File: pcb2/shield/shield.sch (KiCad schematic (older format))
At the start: 17 parts, among them IC1 AM26C31CNSR, IC2 AM26C31CNSR, P1 ARD_NW, P10 BUS5, P11 BUS6, P12 BUS7, P13 BUS8, P2 ARD_SW, P3 ARD_NE, P4 ARD_SE, P5 SHIFT, P6 BUS1, P7 BUS2, P8 BUS3, P9 BUS4

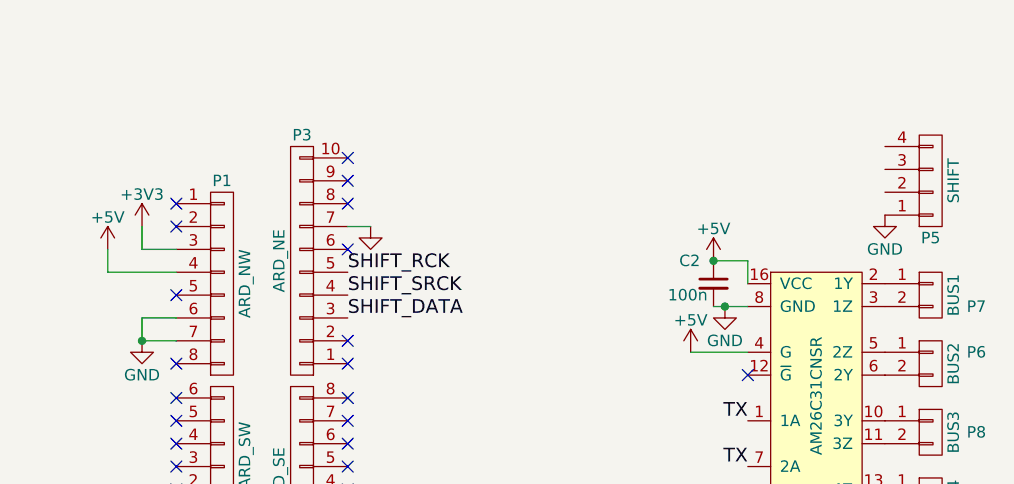
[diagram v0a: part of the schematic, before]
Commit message: Added SHIFT connections, sated ERC
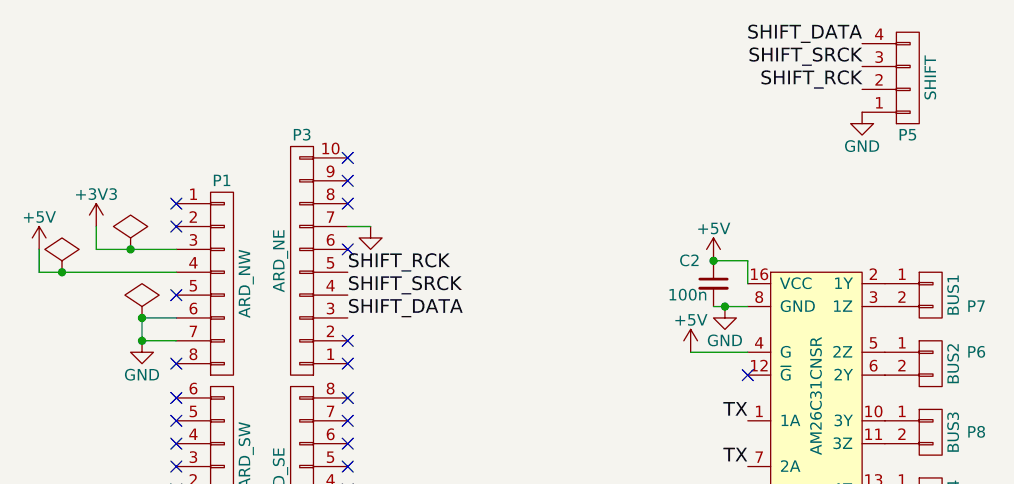
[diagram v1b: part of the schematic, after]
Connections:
- net SHIFT_DATA: now also P5.4 (P4)
- net SHIFT_RCK: now also P5.2 (P2)
- net SHIFT_SRCK: now also P5.3 (P3)
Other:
- moved on the sheet: P5
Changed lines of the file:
@@
 L +3V3 #PWR01
 U 1 1 56F8546D
-P 2150 2000
-F 0 "#PWR01" H 2150 1850 50  0001 C CNN
-F 1 "+3V3" H 2150 2140 50  0000 C CNN
-F 2 "" H 2150 2000 50  0000 C CNN
-F 3 "" H 2150 2000 50  0000 C CNN
-	1    2150 2000
-	1    0    0    -1
-$EndComp
-Wire Wire Line
-	2150 2000 2150 2100
-Wire Wire Line
-	2150 2100 2300 2100
+P 1950 2000
+F 0 "#PWR01" H 1950 1850 50  0001 C CNN
+F 1 "+3V3" H 1950 2140 50  0000 C CNN
+F 2 "" H 1950 2000 50  0000 C CNN
+F 3 "" H 1950 2000 50  0000 C CNN
+	1    1950 2000
+	1    0    0    -1
+$EndComp
+Wire Wire Line
+	1950 2000 1950 2100
+Wire Wire Line
+	1950 2100 2300 2100
 $Comp
 L +5V #PWR02
 U 1 1 56F85493
-P 2000 2100
-F 0 "#PWR02" H 2000 1950 50  0001 C CNN
-F 1 "+5V" H 2000 2240 50  0000 C CNN
-F 2 "" H 2000 2100 50  0000 C CNN
-F 3 "" H 2000 2100 50  0000 C CNN
-	1    2000 2100
-	1    0    0    -1
-$EndComp
-Wire Wire Line
-	2000 2100 2000 2200
-Wire Wire Line
-	2000 2200 2300 2200
+P 1700 2100
+F 0 "#PWR02" H 1700 1950 50  0001 C CNN
+F 1 "+5V" H 1700 2240 50  0000 C CNN
+F 2 "" H 1700 2100 50  0000 C CNN
+F 3 "" H 1700 2100 50  0000 C CNN
+	1    1700 2100
+	1    0    0    -1
+$EndComp
+Wire Wire Line
+	1700 2100 1700 2200
+Wire Wire Line
+	1700 2200 2300 2200
 $Comp
 L GND #PWR03
@@
 L CONN_01X04 P5
 U 1 1 56F855FD
-P 5600 1800
-F 0 "P5" H 5600 2050 50  0000 C CNN
-F 1 "SHIFT" V 5700 1800 50  0000 C CNN
-F 2 "Pin_Headers:Pin_Header_Straight_1x04" H 5600 1800 50  0001 C CNN
-F 3 "" H 5600 1800 50  0000 C CNN
-	1    5600 1800
+P 5500 1350
+F 0 "P5" H 5500 1600 50  0000 C CNN
+F 1 "SHIFT" V 5600 1350 50  0000 C CNN
+F 2 "Pin_Headers:Pin_Header_Straight_1x04" H 5500 1350 50  0001 C CNN
+F 3 "" H 5500 1350 50  0000 C CNN
+	1    5500 1350
 	1    0    0    1
 $EndComp
@@
 L GND #PWR05
 U 1 1 56F85F2A
-P 5400 1950
-F 0 "#PWR05" H 5400 1700 50  0001 C CNN
-F 1 "GND" H 5400 1800 50  0000 C CNN
-F 2 "" H 5400 1950 50  0000 C CNN
-F 3 "" H 5400 1950 50  0000 C CNN
-	1    5400 1950
+P 5300 1500
+F 0 "#PWR05" H 5300 1250 50  0001 C CNN
+F 1 "GND" H 5300 1350 50  0000 C CNN
+F 2 "" H 5300 1500 50  0000 C CNN
+F 3 "" H 5300 1500 50  0000 C CNN
+	1    5300 1500
 	1    0    0    -1
 $EndComp
@@
 	4550 3500 4550 3600
 Connection ~ 4700 3700
+Text Label 5300 1400 2    60   ~ 0
+SHIFT_RCK
+Text Label 5300 1300 2    60   ~ 0
+SHIFT_SRCK
+Text Label 5300 1200 2    60   ~ 0
+SHIFT_DATA
+$Comp
+L PWR_FLAG #FLG012
+U 1 1 56F87626
+P 2100 2100
+F 0 "#FLG012" H 2100 2195 50  0001 C CNN
+F 1 "PWR_FLAG" H 2100 2280 50  0001 C CNN
+F 2 "" H 2100 2100 50  0000 C CNN
+F 3 "" H 2100 2100 50  0000 C CNN
+	1    2100 2100
+	1    0    0    -1
+$EndComp
+Connection ~ 2100 2100
+$Comp
+L PWR_FLAG #FLG013
+U 1 1 56F87848
+P 2150 2400
+F 0 "#FLG013" H 2150 2495 50  0001 C CNN
+F 1 "PWR_FLAG" H 2150 2580 50  0001 C CNN
+F 2 "" H 2150 2400 50  0000 C CNN
+F 3 "" H 2150 2400 50  0000 C CNN
+	1    2150 2400
+	1    0    0    -1
+$EndComp
+Connection ~ 2150 2400
+$Comp
+L PWR_FLAG #FLG014
+U 1 1 56F87AC1
+P 1800 2200
+F 0 "#FLG014" H 1800 2295 50  0001 C CNN
+F 1 "PWR_FLAG" H 1800 2380 50  0001 C CNN
+F 2 "" H 1800 2200 50  0000 C CNN
+F 3 "" H 1800 2200 50  0000 C CNN
+	1    1800 2200
+	1    0    0    -1
+$EndComp
+Connection ~ 1800 2200
 $EndSCHEMATC

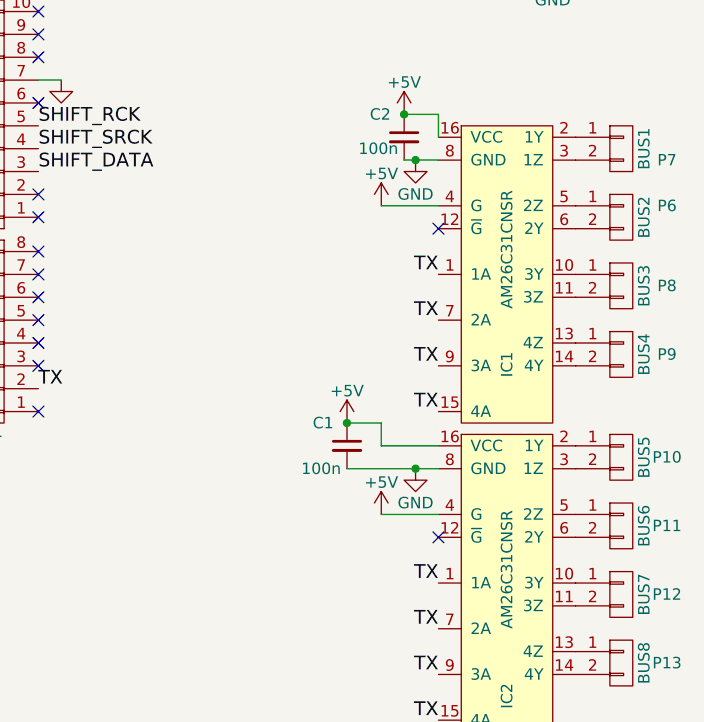
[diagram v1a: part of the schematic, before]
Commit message: Proof of concept route of shield
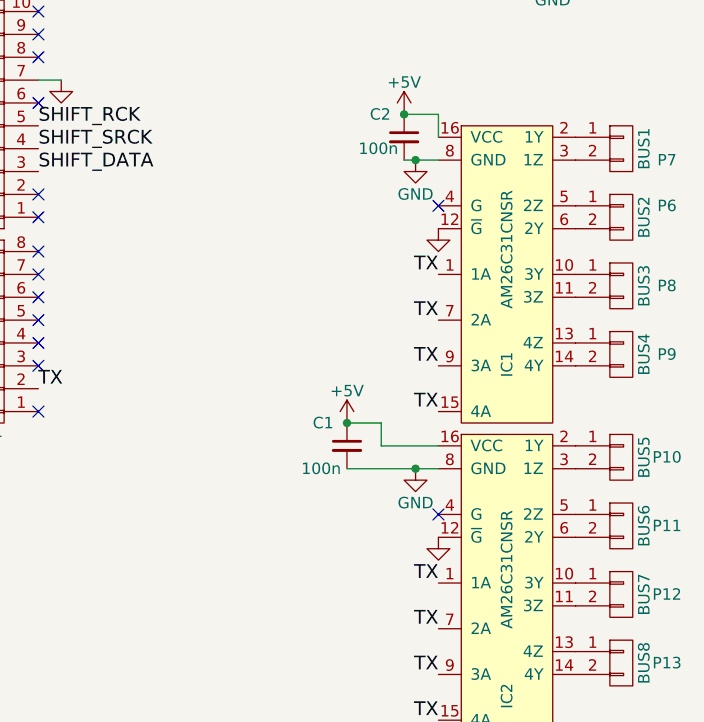
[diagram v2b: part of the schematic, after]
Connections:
- net +5V: no longer IC1.4 (G), IC2.4 (G)
- net GND: now also IC1.12 (~G), IC2.12 (~G)
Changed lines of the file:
@@
 Wire Wire Line
 	4650 2350 4800 2350
-Wire Wire Line
-	4800 2550 4550 2550
-$Comp
-L +5V #PWR08
-U 1 1 56F86E14
-P 4550 2550
-F 0 "#PWR08" H 4550 2400 50  0001 C CNN
-F 1 "+5V" H 4550 2690 50  0000 C CNN
-F 2 "" H 4550 2550 50  0000 C CNN
-F 3 "" H 4550 2550 50  0000 C CNN
-	1    4550 2550
-	1    0    0    -1
-$EndComp
 $Comp
 L +5V #PWR09
@@
 Wire Wire Line
 	4400 3700 4800 3700
-Wire Wire Line
-	4800 3900 4550 3900
-$Comp
-L +5V #PWR011
-U 1 1 56F86F7D
-P 4550 3900
-F 0 "#PWR011" H 4550 3750 50  0001 C CNN
-F 1 "+5V" H 4550 4040 50  0000 C CNN
-F 2 "" H 4550 3900 50  0000 C CNN
-F 3 "" H 4550 3900 50  0000 C CNN
-	1    4550 3900
-	1    0    0    -1
-$EndComp
-NoConn ~ 4800 2650
-NoConn ~ 4800 4000
 Text Label 4800 2850 2    60   ~ 0
 TX
@@
 $EndComp
 Connection ~ 1800 2200
+NoConn ~ 4800 2550
+$Comp
+L GND #PWR?
+U 1 1 56F87C8E
+P 4800 2650
+F 0 "#PWR?" H 4800 2400 50  0001 C CNN
+F 1 "GND" H 4800 2500 50  0001 C CNN
+F 2 "" H 4800 2650 50  0000 C CNN
+F 3 "" H 4800 2650 50  0000 C CNN
+	1    4800 2650
+	1    0    0    -1
+$EndComp
+$Comp
+L GND #PWR?
+U 1 1 56F87D9A
+P 4800 4000
+F 0 "#PWR?" H 4800 3750 50  0001 C CNN
+F 1 "GND" H 4800 3850 50  0001 C CNN
+F 2 "" H 4800 4000 50  0000 C CNN
+F 3 "" H 4800 4000 50  0000 C CNN
+	1    4800 4000
+	1    0    0    -1
+$EndComp
+NoConn ~ 4800 3900
 $EndSCHEMATC

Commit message: Added part numbers and BOMs
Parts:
- C1, C2: Farnell (none) -> 2496833
- P10, P11, P12, P13, P6, P7, P8, P9: Farnell (none) -> 1830747
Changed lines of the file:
@@
 F 2 "agg:S02B-PASK-2" H 5600 2300 50  0001 C CNN
 F 3 "" H 5600 2300 50  0000 C CNN
+F 4 "1830747" H 5600 2300 60  0001 C CNN "Farnell"
 	1    5600 2300
 	1    0    0    -1
@@
 F 2 "agg:S02B-PASK-2" H 5600 2600 50  0001 C CNN
 F 3 "" H 5600 2600 50  0000 C CNN
+F 4 "1830747" H 5600 2600 60  0001 C CNN "Farnell"
 	1    5600 2600
 	1    0    0    -1
@@
 F 2 "agg:S02B-PASK-2" H 5600 2900 50  0001 C CNN
 F 3 "" H 5600 2900 50  0000 C CNN
+F 4 "1830747" H 5600 2900 60  0001 C CNN "Farnell"
 	1    5600 2900
 	1    0    0    -1
@@
 F 2 "agg:S02B-PASK-2" H 5600 3200 50  0001 C CNN
 F 3 "" H 5600 3200 50  0000 C CNN
+F 4 "1830747" H 5600 3200 60  0001 C CNN "Farnell"
 	1    5600 3200
 	1    0    0    -1
@@
 F 2 "agg:S02B-PASK-2" H 5600 3650 50  0001 C CNN
 F 3 "" H 5600 3650 50  0000 C CNN
+F 4 "1830747" H 5600 3650 60  0001 C CNN "Farnell"
 	1    5600 3650
 	1    0    0    -1
@@
 F 2 "agg:S02B-PASK-2" H 5600 3950 50  0001 C CNN
 F 3 "" H 5600 3950 50  0000 C CNN
+F 4 "1830747" H 5600 3950 60  0001 C CNN "Farnell"
 	1    5600 3950
 	1    0    0    -1
@@
 F 2 "agg:S02B-PASK-2" H 5600 4250 50  0001 C CNN
 F 3 "" H 5600 4250 50  0000 C CNN
+F 4 "1830747" H 5600 4250 60  0001 C CNN "Farnell"
 	1    5600 4250
 	1    0    0    -1
@@
 F 2 "agg:S02B-PASK-2" H 5600 4550 50  0001 C CNN
 F 3 "" H 5600 4550 50  0000 C CNN
+F 4 "1830747" H 5600 4550 60  0001 C CNN "Farnell"
 	1    5600 4550
 	1    0    0    -1
@@
 F 2 "agg:0603" H 4650 2250 50  0001 C CNN
 F 3 "" H 4650 2250 50  0000 C CNN
+F 4 "2496833" H 4650 2250 60  0001 C CNN "Farnell"
 	1    4650 2250
 	1    0    0    -1
@@
 F 2 "agg:0603" H 4400 3600 50  0001 C CNN
 F 3 "" H 4400 3600 50  0000 C CNN
+F 4 "2496833" H 4400 3600 60  0001 C CNN "Farnell"
 	1    4400 3600
 	1    0    0    -1

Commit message: Repsin of new shield PCB, nominal first route.
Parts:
- removed IC1, IC2: AM26C31CNSR, agg:SOIC-16, symbol AM26C31CNSR
- removed P1: ARD_NW, Pin_Headers:Pin_Header_Straight_1x08, symbol CONN_01X08
- removed P2: ARD_SW, Pin_Headers:Pin_Header_Straight_1x06, symbol CONN_01X06
- removed P3: ARD_NE, Pin_Headers:Pin_Header_Straight_1x10, symbol CONN_01X10
- removed P4: ARD_SE, Pin_Headers:Pin_Header_Straight_1x08, symbol CONN_01X08
- added C10, C7, C9: 1u, agg:0603, symbol C
- added C3, C6, C8: 100n, agg:0603, symbol C
- added C4: 10u, agg:0603, symbol C
- added C5: C, agg:0603, symbol C
- added IC1: STM32F0xxKxTx, agg:LQFP-32, symbol STM32F0xxKxTx
- added IC2: MCP1700, agg:SOT-23, symbol MCP1700
- added IC3, IC4: AM26C31, agg:SOIC-16, symbol AM26C31
- added J1: MICROUSB, agg:MICROUSB_MOLEX_47589-0001, symbol MICROUSB
- added P?: SWD_TC, agg:TC2030-NL, symbol SWD_TC
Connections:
- net +3V3: now also C10.1, C3.1, C4.1, C6.1, C7.1, C8.1, IC1.1 (VDD), IC1.17 (VDD), IC1.5 (VDDA), IC2.2 (VOUT), P?.1 (VDD)
- net +5V: now also C9.1, IC2.3 (VIN), IC3.16 (VCC), IC4.16 (VCC), J1.1 (VCC)
- net GND: now also C10.2, C3.2, C4.2, C5.2, C6.2, C7.2, C8.2, C9.2, IC1.16 (VSS), IC1.31 (BOOT0), IC1.32 (VSS), IC2.1 (GND), IC3.12 (~G), IC3.8 (GND), IC4.12 (~G), IC4.8 (GND), J1.5 (GND), P?.5 (GND)
- net SHIFT_DATA: now also IC1.13 (PA7)
- net SHIFT_RCK: now also IC1.11 (PA5)
- net SHIFT_SRCK: now also IC1.12 (PA6)
- net TX: now also IC1.8 (PA2), IC3.1 (1A), IC3.15 (4A), IC3.7 (2A), IC3.9 (3A), IC4.1 (1A), IC4.15 (4A), IC4.7 (2A), IC4.9 (3A)
- net at P6.1 (P1): now also IC3.2 (1Y)
- net at P6.2 (P2): now also IC3.3 (1Z)
- net at P7.1 (P1): now also IC3.6 (2Y)
- net at P7.2 (P2): now also IC3.5 (2Z)
- net at P8.1 (P1): now also IC3.10 (3Y)
- net at P8.2 (P2): now also IC3.11 (3Z)
- net at P9.1 (P1): now also IC3.14 (4Y)
- net at P9.2 (P2): now also IC3.13 (4Z)
- net at P10.1 (P1): now also IC4.2 (1Y)
- net at P10.2 (P2): now also IC4.3 (1Z)
- net at P11.1 (P1): now also IC4.6 (2Y)
- net at P11.2 (P2): now also IC4.5 (2Z)
- net at P12.1 (P1): now also IC4.10 (3Y)
- net at P12.2 (P2): now also IC4.11 (3Z)
- net at P13.1 (P1): now also IC4.14 (4Y)
- net at P13.2 (P2): now also IC4.13 (4Z)
- new net SWDCLK: IC1.24 (PA14), P?.4 (SWDCLK)
- new net SWDIO: IC1.23 (PA13), P?.2 (SWDIO)
- new net USB_D+: IC1.22 (PA12), J1.3 (D+)
- new net USB_D-: IC1.21 (PA11), J1.2 (D-)
- new net nRST: C5.1, IC1.4 (NRST), P?.3 (~RST)
- no-connect marks 25 -> 5
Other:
- note added: "VDD1"
- note added: "VDD2"
- note added: "VDDA"
- moved on the sheet: C1, C2, P10, P11, P12, P13, P5, P6, P7, P8, P9

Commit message: Re-route of shield, DRC issues though.
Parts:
- added X1, X2, X3, X4: PART, agg:M3_MOUNT, symbol PART
- gave numbers to parts that had none: 1
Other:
- note added: "Mounting\nHoles"
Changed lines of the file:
@@
 LIBS:mcp1700
 LIBS:swd_tc
+LIBS:part
 LIBS:shield-cache
 EELAYER 25 0
@@
 $EndComp
 $Comp
-L GND #PWR01
+L GND #PWR30
 U 1 1 56F85F2A
 P 8850 1650
-F 0 "#PWR01" H 8850 1400 50  0001 C CNN
+F 0 "#PWR30" H 8850 1400 50  0001 C CNN
 F 1 "GND" H 8850 1500 50  0000 C CNN
 F 2 "" H 8850 1650 50  0000 C CNN
@@
 $EndComp
 $Comp
-L +5V #PWR02
+L +5V #PWR25
 U 1 1 56F86D5E
 P 8200 2300
-F 0 "#PWR02" H 8200 2150 50  0001 C CNN
+F 0 "#PWR25" H 8200 2150 50  0001 C CNN
 F 1 "+5V" H 8200 2440 50  0000 C CNN
 F 2 "" H 8200 2300 50  0000 C CNN
@@
 $EndComp
 $Comp
-L GND #PWR03
+L GND #PWR26
 U 1 1 56F86DAA
 P 8250 2500
-F 0 "#PWR03" H 8250 2250 50  0001 C CNN
+F 0 "#PWR26" H 8250 2250 50  0001 C CNN
 F 1 "GND" H 8250 2350 50  0000 C CNN
 F 2 "" H 8250 2500 50  0000 C CNN
@@
 $EndComp
 $Comp
-L +5V #PWR04
+L +5V #PWR24
 U 1 1 56F86E73
 P 7950 3900
-F 0 "#PWR04" H 7950 3750 50  0001 C CNN
+F 0 "#PWR24" H 7950 3750 50  0001 C CNN
 F 1 "+5V" H 7950 4040 50  0000 C CNN
 F 2 "" H 7950 3900 50  0000 C CNN
@@
 $EndComp
 $Comp
-L GND #PWR05
+L GND #PWR27
 U 1 1 56F86EC2
 P 8250 4100
-F 0 "#PWR05" H 8250 3850 50  0001 C CNN
+F 0 "#PWR27" H 8250 3850 50  0001 C CNN
 F 1 "GND" H 8250 3950 50  0000 C CNN
 F 2 "" H 8250 4100 50  0000 C CNN
@@
 NoConn ~ 8350 2700
 $Comp
-L GND #PWR06
+L GND #PWR28
 U 1 1 56F87C8E
 P 8350 2800
-F 0 "#PWR06" H 8350 2550 50  0001 C CNN
+F 0 "#PWR28" H 8350 2550 50  0001 C CNN
 F 1 "GND" H 8350 2650 50  0001 C CNN
 F 2 "" H 8350 2800 50  0000 C CNN
@@
 $EndComp
 $Comp
-L GND #PWR07
+L GND #PWR29
 U 1 1 56F87D9A
 P 8350 4400
-F 0 "#PWR07" H 8350 4150 50  0001 C CNN
+F 0 "#PWR29" H 8350 4150 50  0001 C CNN
 F 1 "GND" H 8350 4250 50  0001 C CNN
 F 2 "" H 8350 4400 50  0000 C CNN
@@
 $EndComp
 $Comp
-L +5V #PWR08
+L +5V #PWR15
 U 1 1 5794B897
 P 4550 1300
-F 0 "#PWR08" H 4550 1150 50  0001 C CNN
+F 0 "#PWR15" H 4550 1150 50  0001 C CNN
 F 1 "+5V" H 4565 1473 50  0000 C CNN
 F 2 "" H 4550 1300 50  0000 C CNN
@@
 $EndComp
 $Comp
-L GND #PWR09
+L GND #PWR16
 U 1 1 5794B8F4
 P 4600 1950
-F 0 "#PWR09" H 4600 1700 50  0001 C CNN
+F 0 "#PWR16" H 4600 1700 50  0001 C CNN
 F 1 "GND" H 4605 1777 50  0000 C CNN
 F 2 "" H 4600 1950 50  0000 C CNN
@@
 $EndComp
 $Comp
-L +3V3 #PWR010
+L +3V3 #PWR12
 U 1 1 5794BB55
 P 2500 3200
-F 0 "#PWR010" H 2500 3050 50  0001 C CNN
+F 0 "#PWR12" H 2500 3050 50  0001 C CNN
 F 1 "+3V3" H 2515 3373 50  0000 C CNN
 F 2 "" H 2500 3200 50  0000 C CNN
@@
 $EndComp
 $Comp
-L GND #PWR011
+L GND #PWR9
 U 1 1 5794BBFE
 P 2400 3550
-F 0 "#PWR011" H 2400 3300 50  0001 C CNN
+F 0 "#PWR9" H 2400 3300 50  0001 C CNN
 F 1 "GND" H 2405 3377 50  0000 C CNN
 F 2 "" H 2400 3550 50  0000 C CNN
@@
 $EndComp
 $Comp
-L GND #PWR012
+L GND #PWR5
 U 1 1 5794BE19
 P 1850 4150
-F 0 "#PWR012" H 1850 3900 50  0001 C CNN
+F 0 "#PWR5" H 1850 3900 50  0001 C CNN
 F 1 "GND" H 1855 3977 50  0000 C CNN
 F 2 "" H 1850 4150 50  0000 C CNN
@@
 nRST
 $Comp
-L GND #PWR013
+L GND #PWR8
 U 1 1 5794BF98
 P 2150 3950
-F 0 "#PWR013" H 2150 3700 50  0001 C CNN
+F 0 "#PWR8" H 2150 3700 50  0001 C CNN
 F 1 "GND" H 2155 3777 50  0000 C CNN
 F 2 "" H 2150 3950 50  0000 C CNN
@@
 $EndComp
 $Comp
-L +3V3 #PWR014
+L +3V3 #PWR1
 U 1 1 5794C2DC
 P 1350 900
-F 0 "#PWR014" H 1350 750 50  0001 C CNN
+F 0 "#PWR1" H 1350 750 50  0001 C CNN
 F 1 "+3V3" H 1365 1073 50  0000 C CNN
 F 2 "" H 1350 900 50  0000 C CNN
@@
 $EndComp
 $Comp
-L +3V3 #PWR015
+L +3V3 #PWR3
 U 1 1 5794C329
 P 1750 900
-F 0 "#PWR015" H 1750 750 50  0001 C CNN
+F 0 "#PWR3" H 1750 750 50  0001 C CNN
 F 1 "+3V3" H 1765 1073 50  0000 C CNN
 F 2 "" H 1750 900 50  0000 C CNN
@@
 $EndComp
 $Comp
-L +3V3 #PWR016
+L +3V3 #PWR6
 U 1 1 5794C376
 P 2100 900
-F 0 "#PWR016" H 2100 750 50  0001 C CNN
+F 0 "#PWR6" H 2100 750 50  0001 C CNN
 F 1 "+3V3" H 2115 1073 50  0000 C CNN
 F 2 "" H 2100 900 50  0000 C CNN
@@
 $EndComp
 $Comp
-L GND #PWR017
+L GND #PWR2
 U 1 1 5794C3C3
 P 1350 1200
-F 0 "#PWR017" H 1350 950 50  0001 C CNN
+F 0 "#PWR2" H 1350 950 50  0001 C CNN
 F 1 "GND" H 1355 1027 50  0000 C CNN
 F 2 "" H 1350 1200 50  0000 C CNN
@@
 $EndComp
 $Comp
-L GND #PWR018
+L GND #PWR4
 U 1 1 5794C410
 P 1750 1200
-F 0 "#PWR018" H 1750 950 50  0001 C CNN
+F 0 "#PWR4" H 1750 950 50  0001 C CNN
 F 1 "GND" H 1755 1027 50  0000 C CNN
 F 2 "" H 1750 1200 50  0000 C CNN
@@
 $EndComp
 $Comp
-L GND #PWR019
+L GND #PWR7
 U 1 1 5794C45D
 P 2100 1200
-F 0 "#PWR019" H 2100 950 50  0001 C CNN
+F 0 "#PWR7" H 2100 950 50  0001 C CNN
 F 1 "GND" H 2105 1027 50  0000 C CNN
 F 2 "" H 2100 1200 50  0000 C CNN
@@
 $EndComp
 $Comp
-L +3V3 #PWR020
+L +3V3 #PWR10
 U 1 1 5794C73B
 P 2500 900
-F 0 "#PWR020" H 2500 750 50  0001 C CNN
+F 0 "#PWR10" H 2500 750 50  0001 C CNN
 F 1 "+3V3" H 2515 1073 50  0000 C CNN
 F 2 "" H 2500 900 50  0000 C CNN
@@
 $EndComp
 $Comp
-L +3V3 #PWR021
+L +3V3 #PWR13
 U 1 1 5794C78E
 P 2800 900
-F 0 "#PWR021" H 2800 750 50  0001 C CNN
+F 0 "#PWR13" H 2800 750 50  0001 C CNN
 F 1 "+3V3" H 2815 1073 50  0000 C CNN
 F 2 "" H 2800 900 50  0000 C CNN
@@
 $EndComp
 $Comp
-L GND #PWR022
+L GND #PWR11
 U 1 1 5794C7E1
 P 2500 1200
-F 0 "#PWR022" H 2500 950 50  0001 C CNN
+F 0 "#PWR11" H 2500 950 50  0001 C CNN
 F 1 "GND" H 2505 1027 50  0000 C CNN
 F 2 "" H 2500 1200 50  0000 C CNN
@@
 $EndComp
 $Comp
-L GND #PWR023
+L GND #PWR14
 U 1 1 5794C834
 P 2800 1200
-F 0 "#PWR023" H 2800 950 50  0001 C CNN
+F 0 "#PWR14" H 2800 950 50  0001 C CNN
 F 1 "GND" H 2805 1027 50  0000 C CNN
 F 2 "" H 2800 1200 50  0000 C CNN
@@
 $EndComp
 $Comp
-L GND #PWR024
+L GND #PWR21
 U 1 1 5794D178
 P 6000 1450
-F 0 "#PWR024" H 6000 1200 50  0001 C CNN
+F 0 "#PWR21" H 6000 1200 50  0001 C CNN
 F 1 "GND" H 6005 1277 50  0000 C CNN
 F 2 "" H 6000 1450 50  0000 C CNN
@@
 	2150 3950 2600 3950
 $Comp
-L +5V #PWR025
+L +5V #PWR19
 U 1 1 5794D32F
 P 5600 1350
-F 0 "#PWR025" H 5600 1200 50  0001 C CNN
+F 0 "#PWR19" H 5600 1200 50  0001 C CNN
 F 1 "+5V" H 5615 1523 50  0000 C CNN
 F 2 "" H 5600 1350 50  0000 C CNN
@@
 Connection ~ 5600 1350
 $Comp
-L GND #PWR026
+L GND #PWR20
 U 1 1 5794D41F
 P 5600 1650
-F 0 "#PWR026" H 5600 1400 50  0001 C CNN
+F 0 "#PWR20" H 5600 1400 50  0001 C CNN
 F 1 "GND" H 5605 1477 50  0000 C CNN
 F 2 "" H 5600 1650 50  0000 C CNN
@@
 $EndComp
 $Comp
-L +3V3 #PWR027
+L +3V3 #PWR22
 U 1 1 5794D4F1
 P 6900 1350
-F 0 "#PWR027" H 6900 1200 50  0001 C CNN
+F 0 "#PWR22" H 6900 1200 50  0001 C CNN
 F 1 "+3V3" H 6915 1523 50  0000 C CNN
 F 2 "" H 6900 1350 50  0000 C CNN
@@
 Connection ~ 6900 1350
 $Comp
-L GND #PWR028
+L GND #PWR23
 U 1 1 5794D58E
 P 6900 1650
-F 0 "#PWR028" H 6900 1400 50  0001 C CNN
+F 0 "#PWR23" H 6900 1400 50  0001 C CNN
 F 1 "GND" H 6905 1477 50  0000 C CNN
 F 2 "" H 6900 1650 50  0000 C CNN
@@
 SHIFT_RCK
 $Comp
-L SWD_TC P?
+L SWD_TC P1
 U 1 1 5794F816
 P 5850 5300
-F 0 "P?" H 5850 5625 50  0000 C CNN
+F 0 "P1" H 5850 5625 50  0000 C CNN
 F 1 "SWD_TC" H 5850 5534 50  0000 C CNN
 F 2 "agg:TC2030-NL" H 5550 5000 50  0001 L CNN
@@
 $EndComp
 $Comp
-L +3V3 #PWR?
+L +3V3 #PWR17
 U 1 1 5794F9F0
 P 5450 5200
-F 0 "#PWR?" H 5450 5050 50  0001 C CNN
+F 0 "#PWR17" H 5450 5050 50  0001 C CNN
 F 1 "+3V3" H 5465 5373 50  0000 C CNN
 F 2 "" H 5450 5200 50  0000 C CNN
@@
 $EndComp
 $Comp
-L GND #PWR?
+L GND #PWR18
 U 1 1 5794FA4F
 P 5450 5400
-F 0 "#PWR?" H 5450 5150 50  0001 C CNN
+F 0 "#PWR18" H 5450 5150 50  0001 C CNN
 F 1 "GND" H 5455 5227 50  0000 C CNN
 F 2 "" H 5450 5400 50  0000 C CNN
@@
 Text Label 3400 4650 0    60   ~ 0
 SWDCLK
+$Comp
+L PART X1
+U 1 1 57950DA0
+P 850 6600
+F 0 "X1" H 1378 6696 50  0000 L CNN
+F 1 "PART" H 1378 6605 50  0000 L CNN
+F 2 "agg:M3_MOUNT" H 850 6600 50  0001 C CNN
+F 3 "" H 850 6600 50  0001 C CNN
+	1    850  6600
+	1    0    0    -1
+$EndComp
+$Comp
+L PART X2
+U 1 1 57951067
+P 850 6800
+F 0 "X2" H 1378 6896 50  0000 L CNN
+F 1 "PART" H 1378 6805 50  0000 L CNN
+F 2 "agg:M3_MOUNT" H 850 6800 50  0001 C CNN
+F 3 "" H 850 6800 50  0001 C CNN
+	1    850  6800
+	1    0    0    -1
+$EndComp
+$Comp
+L PART X3
+U 1 1 579510D2
+P 850 7000
+F 0 "X3" H 1378 7096 50  0000 L CNN
+F 1 "PART" H 1378 7005 50  0000 L CNN
+F 2 "agg:M3_MOUNT" H 850 7000 50  0001 C CNN
+F 3 "" H 850 7000 50  0001 C CNN
+	1    850  7000
+	1    0    0    -1
+$EndComp
+$Comp
+L PART X4
+U 1 1 579511FE
+P 850 7200
+F 0 "X4" H 1378 7296 50  0000 L CNN
+F 1 "PART" H 1378 7205 50  0000 L CNN
+F 2 "agg:M3_MOUNT" H 850 7200 50  0001 C CNN
+F 3 "" H 850 7200 50  0001 C CNN
+	1    850  7200
+	1    0    0    -1
+$EndComp
+Text Notes 900  6400 0    60   ~ 0
+Mounting\nHoles
 $EndSCHEMATC
